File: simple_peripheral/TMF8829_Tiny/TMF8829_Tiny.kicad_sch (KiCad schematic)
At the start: 0 parts

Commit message: Add TMF8829 symbol library, footprints and power input section
- Library.kicad_sym: TMF8829, C0402, R0402 symbols
- Library.pretty: TMF8829 footprint (embedded Fresnel STEP model),
  0402 capacitor/resistor footprints
- fp-lib-table / sym-lib-table for the local library
- Schematic: 4x 1uF decoupling on VDD/VDDD/VDDC/VDDV, tied to +3.3V

Co-authored-by: Copilot <223556219+Copilot@users.noreply.github.com>
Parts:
- added C1, C2, C3, C4, C5: 1u, Library:C_0402_1005Metric, symbol Library:C0402
- added U1: TMF8829, Library:TMF8829, symbol Library:TMF8829
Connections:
- new net +3.3V: C1.1, C2.1, C3.1, C4.1, C5.1, U1.1 (VDDC), U1.14 (VDDD), U1.16 (VDDV), U1.8 (VDD), U1.9 (VIO)
- new net GND: C1.2, C2.2, C3.2, C4.2, C5.2, U1.15 (GNDV), U1.17 (GND), U1.18 (GND), U1.2 (GNDC), U1.7 (GND)

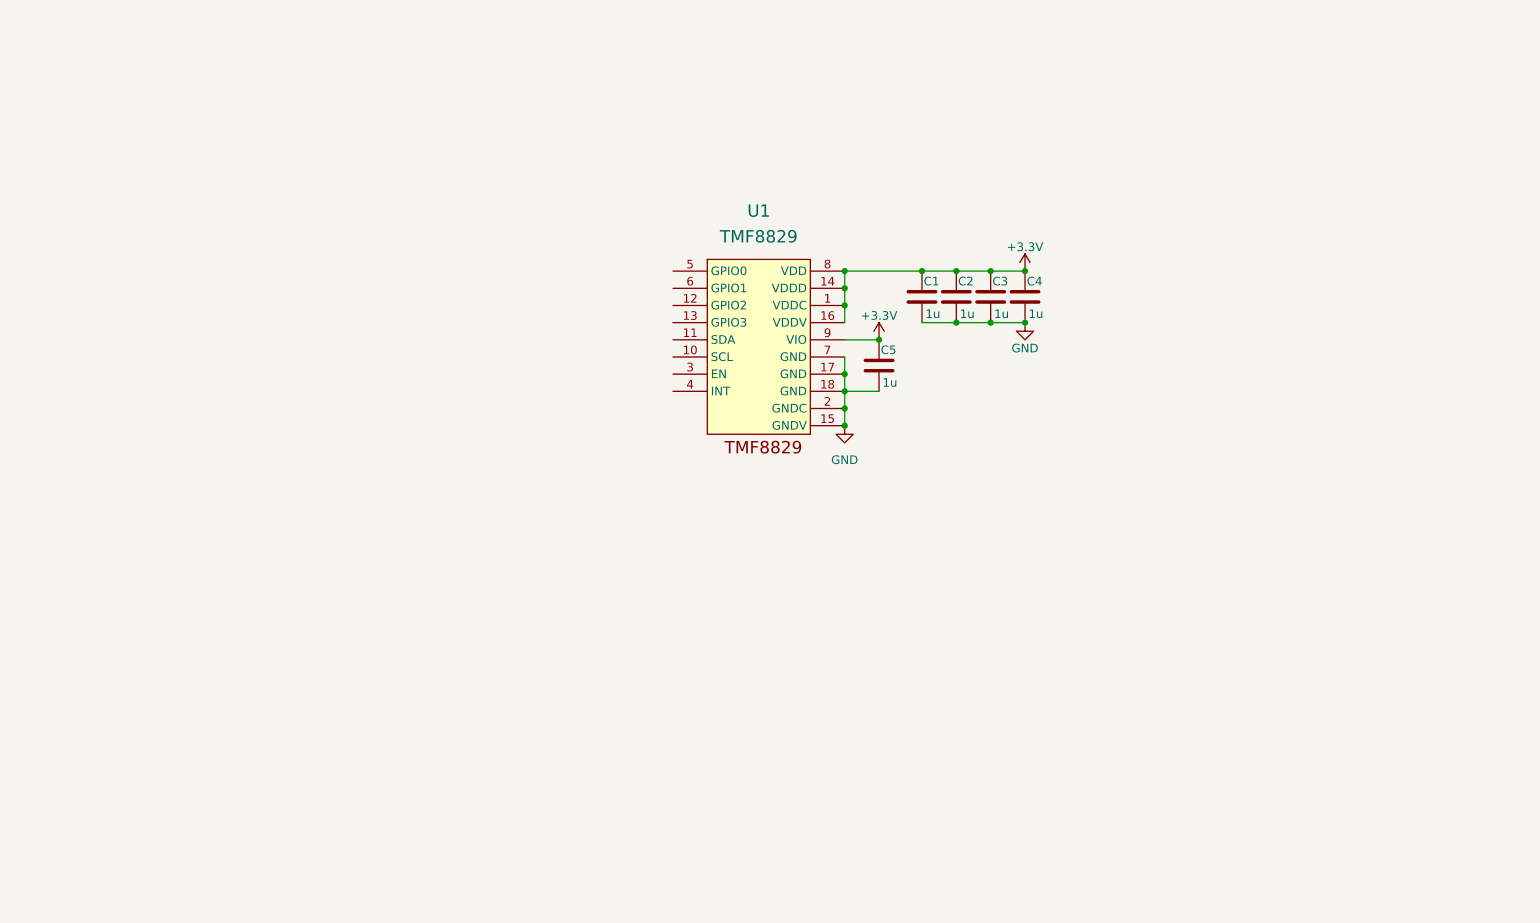
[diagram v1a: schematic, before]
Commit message: Complete TMF8829 Tiny PCB with JLCPCB design rules
- PCB: 4x NPTH M2 mounting holes, 10 extra GND stitching vias,
  test points removed from BOM/position files, footprint values
  aligned with schematic
- Design rules: JLCPCB 2-layer 1oz limits in .kicad_pro
  (0.127mm track/clearance, 0.5/0.3mm via, 0.3mm edge) plus
  .kicad_dru for pad hole, annular ring and hole-to-hole checks
- 3D: all three component models embedded as kicad-embed://,
  no external .3dshapes dependency
- Library: mounting hole, test point, magnetic 6P and GH1.25
  connector footprints; CN1 corrected to SMD; silkscreen removed
  from all footprints (routed to Fab layers instead)
- .gitignore: exclude gerbers, drill files, production output and
  3D model directories

Co-authored-by: Copilot <223556219+Copilot@users.noreply.github.com>
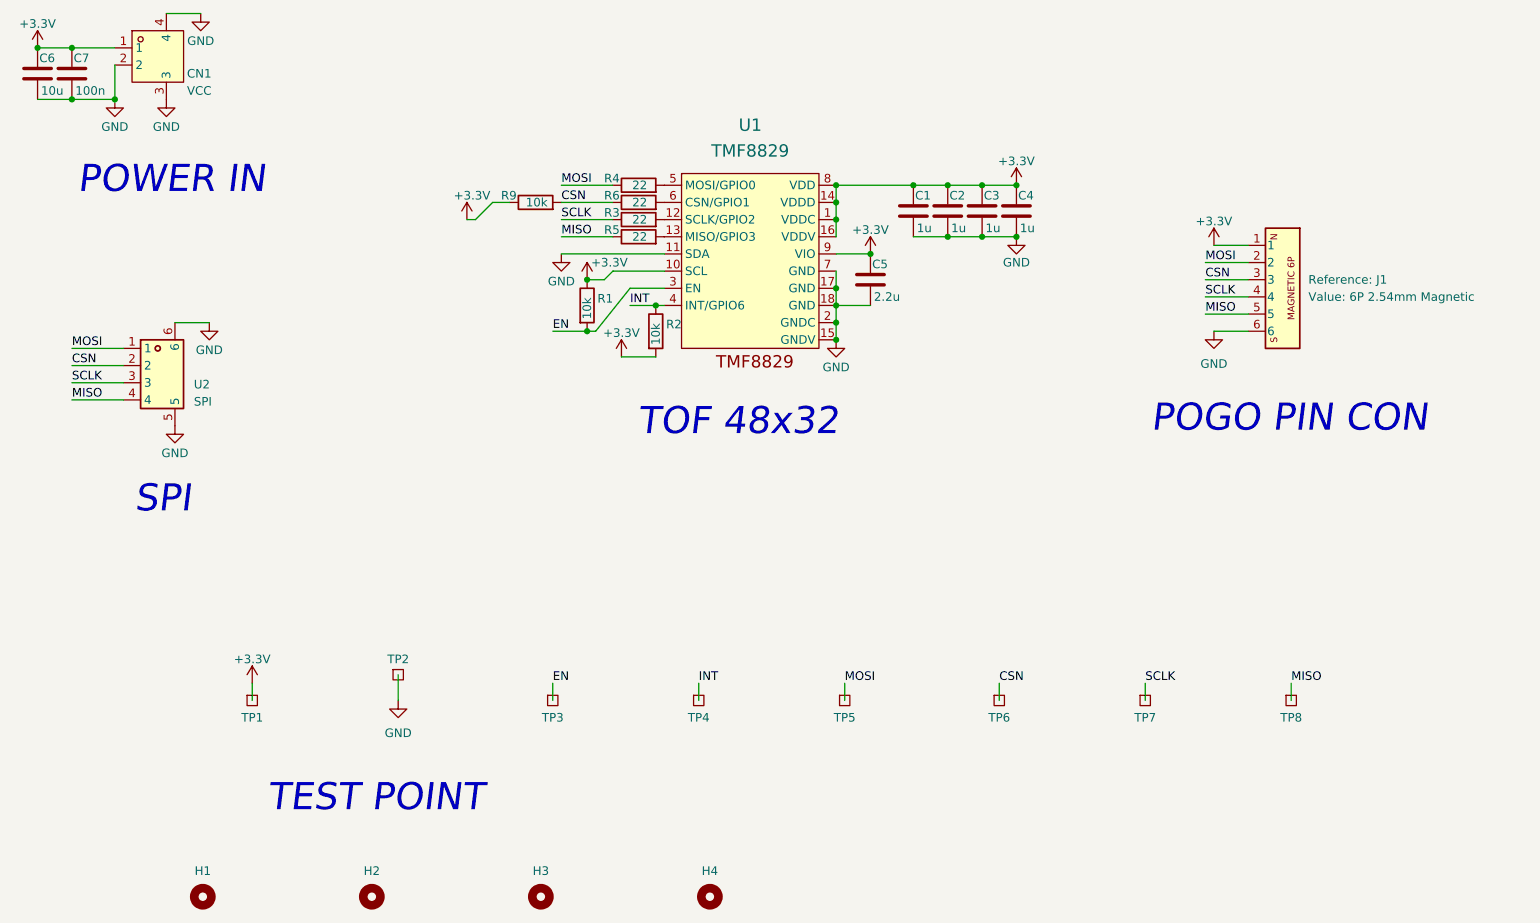
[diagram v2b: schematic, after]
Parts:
- added C6: 10u, Library:C_0402_1005Metric, symbol Library:C0402
- added C7: 100n, Library:C_0402_1005Metric, symbol Library:C0402
- added CN1: VCC, Library:CONN-TH_2P-P1.25_XUNPU_WAFER-GH1.25-2PWB, symbol Library:WAFER-GH1.25-2PWB
- added H1, H2, H3, H4: MountingHole, Library:MountingHole_2.2mm_M2, symbol Library:MountingHole
- added J1: 6P 2.54mm Magnetic, Library:Connector_Magnetic_1x06_P2.54mm_RA, symbol Library:Connector_Magnetic_1x06_P2.54mm
- added R1, R2, R9: 10k, Library:R_0402_1005Metric, symbol Library:R0402
- added R3, R4, R5, R6: 22, Library:R_0402_1005Metric, symbol Library:R0402
- added TP1: 3V3, Library:TestPoint_Pad_2.0x2.0mm, symbol Library:TestPoint_Square
- added TP2: GND, Library:TestPoint_Pad_2.0x2.0mm, symbol Library:TestPoint_Square
- added TP3: EN, Library:TestPoint_Pad_2.0x2.0mm, symbol Library:TestPoint_Square
- added TP4: INT, Library:TestPoint_Pad_2.0x2.0mm, symbol Library:TestPoint_Square
- added TP5: MOSI, Library:TestPoint_Pad_2.0x2.0mm, symbol Library:TestPoint_Square
- added TP6: CSN, Library:TestPoint_Pad_2.0x2.0mm, symbol Library:TestPoint_Square
- added TP7: SCLK, Library:TestPoint_Pad_2.0x2.0mm, symbol Library:TestPoint_Square
- added TP8: MISO, Library:TestPoint_Pad_2.0x2.0mm, symbol Library:TestPoint_Square
- added U2: SPI, Library:CONN-SMD_4P-P1.25_XUNPU_WAFER-GH1.25-4PWB, symbol Library:WAFER-GH1.25-4PWB
- C5: value 1u -> 2.2u
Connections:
- net +3.3V: now also U1.10 (SCL), C6.1, C7.1, CN1.1, J1.1, R1.1, R2.2, R9.1, TP1.1
- net GND: now also U1.11 (SDA), C6.2, C7.2, CN1.2, CN1.3, CN1.4, J1.6, TP2.1, U2.5, U2.6
- net at U1.12 (SCLK/GPIO2): now also R3.2
- net at U1.13 (MISO/GPIO3): now also R5.2
- net EN: now reaches U1.3 (EN)
- net EN: now also R1.2, TP3.1
- net INT: now reaches U1.4 (INT/GPIO6)
- net INT: now also R2.1, TP4.1
- net at U1.5 (MOSI/GPIO0): now also R4.2
- net at U1.6 (CSN/GPIO1): now also R6.2
- new net CSN: J1.3, R6.1, R9.2, TP6.1, U2.2
- new net MISO: J1.5, R5.1, TP8.1, U2.4
- new net MOSI: J1.2, R4.1, TP5.1, U2.1
- new net SCLK: J1.4, R3.1, TP7.1, U2.3
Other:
- note added: "POGO PIN CON"
- note added: "POWER IN"
- note added: "SPI"
- note added: "TEST POINT"
- note added: "TOF 48x32"
- company: (none) -> FireFly WorkShop & sullivan_project
- title: (none) -> TMF_8829_TinY
- moved on the sheet: C1, C2, C3, C4, C5, U1
